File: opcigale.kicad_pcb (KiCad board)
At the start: 2 copper layers, 59.7 x 99.7 mm, 39 parts, among them J1 bat, Q1 2N3904, Q2 2N3904, Q3 2N3904, Q4 2N3904, Q5 2N3906, Q6 2N3904, U1 40106, U4 LM358

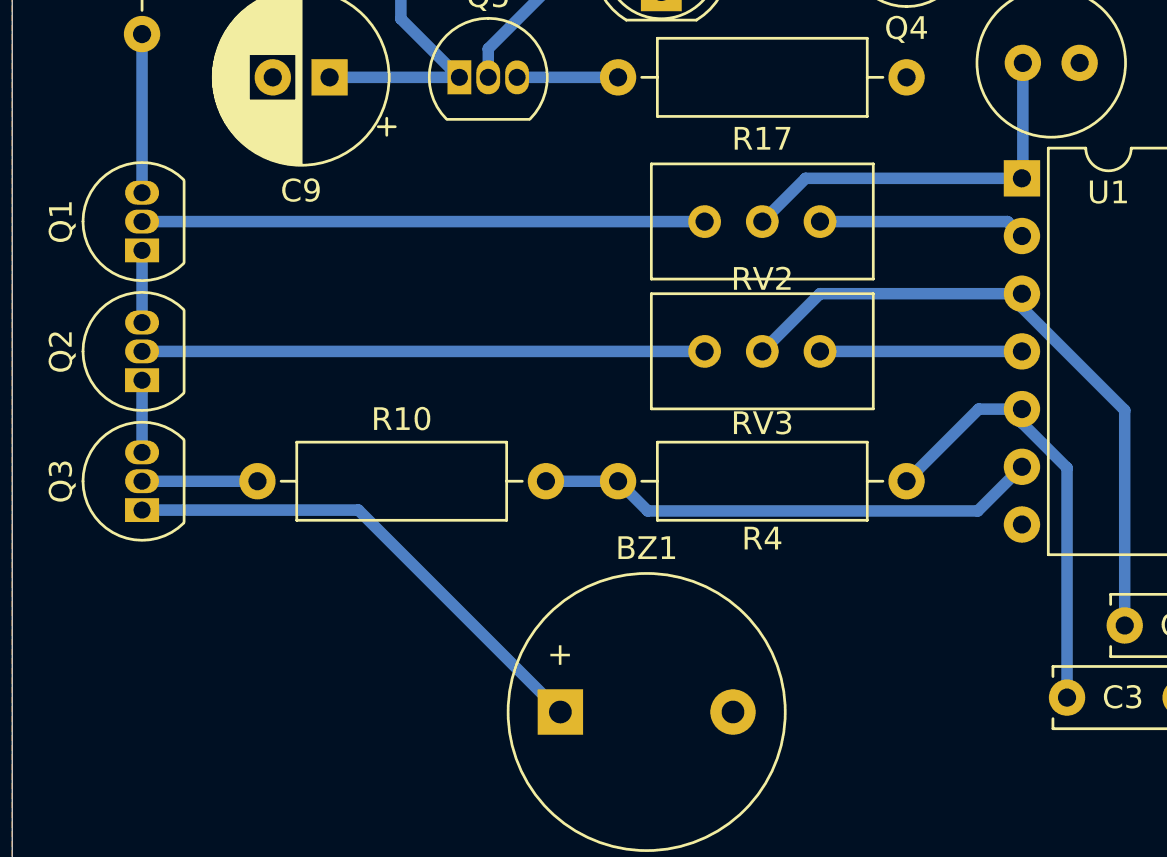
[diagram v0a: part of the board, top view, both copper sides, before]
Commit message: Fix schema/PCB errors, add README
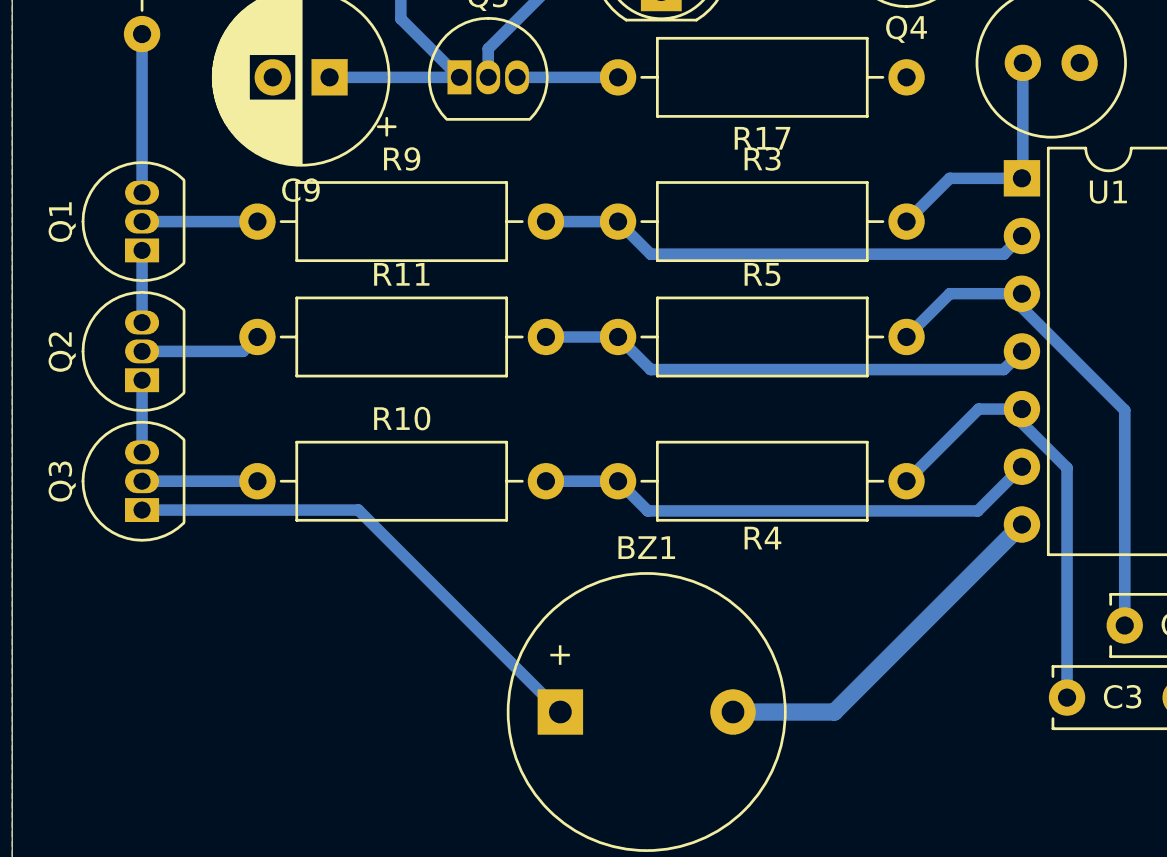
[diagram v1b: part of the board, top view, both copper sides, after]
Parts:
- removed RV2, RV3: R_POT 100k W104, Potentiometer_THT:Potentiometer_Bourns_3296W_Vertical
- added R11: 20k, Resistor_THT:R_Axial_DIN0309_L9.0mm_D3.2mm_P12.70mm_Horizontal, F.Cu at (74.3, 137.8)
- added R3: 48k, Resistor_THT:R_Axial_DIN0309_L9.0mm_D3.2mm_P12.70mm_Horizontal, F.Cu at (90.2, 132.7)
- added R5: 48k, Resistor_THT:R_Axial_DIN0309_L9.0mm_D3.2mm_P12.70mm_Horizontal, F.Cu at (90.2, 137.8)
- added R9: 20k, Resistor_THT:R_Axial_DIN0309_L9.0mm_D3.2mm_P12.70mm_Horizontal, F.Cu at (74.3, 132.7)
- C3: value 0.1uF -> 0.01uF
- C4: value 1uF -> 10uF
- C5: value 100nF -> 1uF
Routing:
- net Net-(Q1-Pad2): track 24.8 -> 5.08 mm
- net Net-(Q2-Pad2): track 24.8 -> 5.34 mm
- net GND: track 0.00 -> 16.1 mm
- net Net-(R11-Pad2): track 8.89 -> 21.9 mm
- net Net-(R3-Pad1): track 9.15 -> 21.9 mm
- net Net-(C2-Pad2): track 29.0 -> 22.3 mm
- net Net-(C1-Pad2): track 17.3 -> 11.0 mm

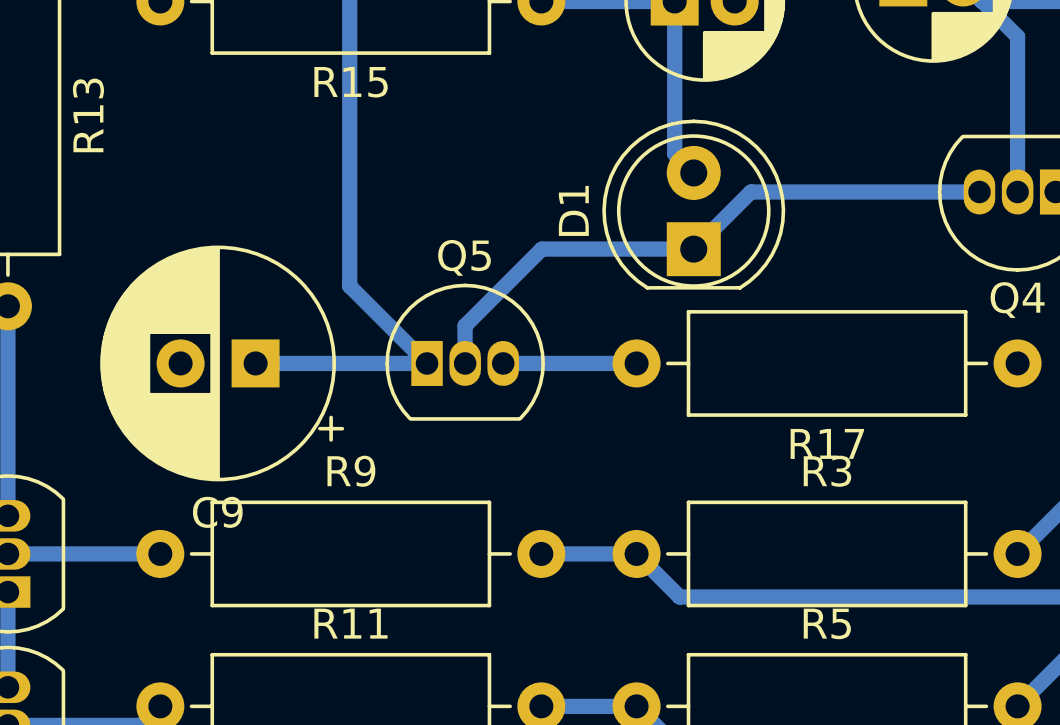
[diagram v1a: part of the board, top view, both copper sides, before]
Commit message: Add opcigale-F_Fab.pdf for assembling ref
Also fix resistor values for oscillators
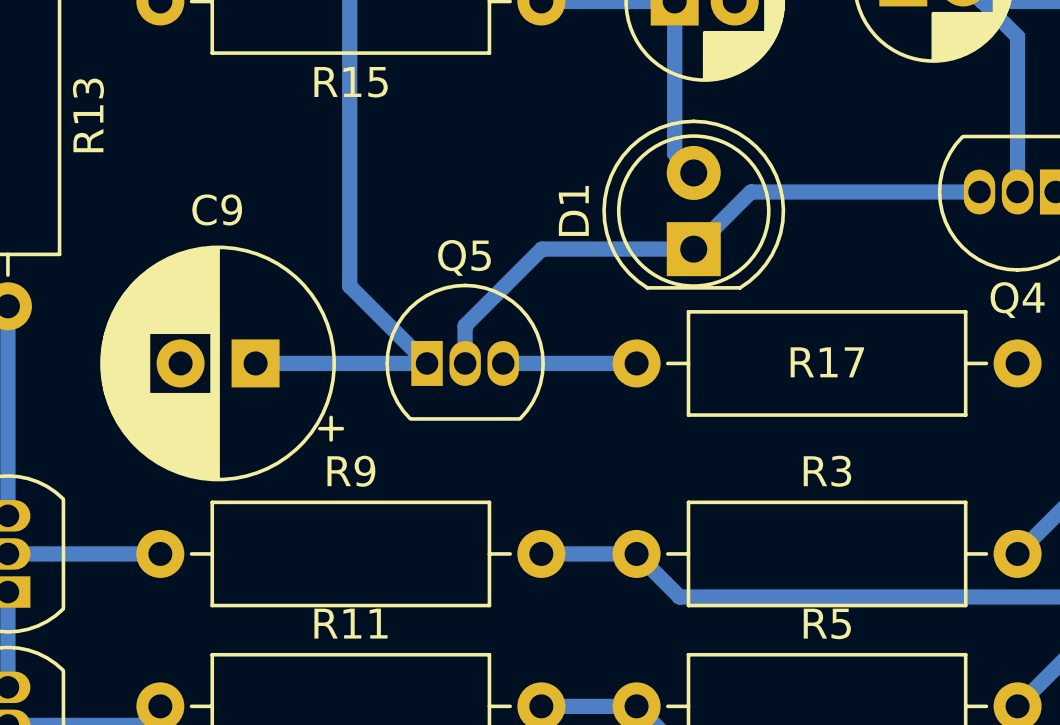
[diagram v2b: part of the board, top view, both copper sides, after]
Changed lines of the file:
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@@
   (layers
     (0 F.Cu signal hide)
-    (31 B.Cu signal)
+    (31 B.Cu signal hide)
     (32 B.Adhes user)
     (33 F.Adhes user)
@@
     (descr "Resistor, Axial_DIN0309 series, Axial, Horizontal, pin pitch=12.7mm, 0.5W = 1/2W, length*diameter=9*3.2mm^2, http://cdn-reichelt.de/documents/datenblatt/B400/1_4W%23YAG.pdf")
     (tags "Resistor Axial_DIN0309 series Axial Horizontal pin pitch 12.7mm 0.5W = 1/2W length 9mm diameter 3.2mm")
-    (fp_text reference R17 (at 6.35 -2.72) (layer F.SilkS)
+    (fp_text reference R17 (at 6.35 0) (layer F.SilkS)
       (effects (font (size 1 1) (thickness 0.15)))
     )
@@
     (descr "CP, Radial series, Radial, pin pitch=2.50mm, , diameter=7.5mm, Electrolytic Capacitor")
     (tags "CP Radial series Radial pin pitch 2.50mm  diameter 7.5mm Electrolytic Capacitor")
-    (fp_text reference C9 (at 1.25 -5) (layer F.SilkS)
-      (effects (font (size 1 1) (thickness 0.15)))
-    )
+    (fp_text reference C9 (at 1.27 5.08) (layer F.SilkS)
+      (effects (font (size 1 1) (thickness 0.15)))
+    )
